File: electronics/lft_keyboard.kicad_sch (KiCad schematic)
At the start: 30 parts, among them SW1 SW_SPST, SW10 SW_SPST, SW11 SW_SPST, SW12 SW_SPST, SW13 SW_SPST, SW14 SW_SPST, SW15 SW_SPST, SW16 SW_SPST, SW17 SW_SPST, SW18 SW_SPST, SW19 SW_SPST, SW2 SW_SPST, SW20 SW_SPST, SW21 SW_SPST, SW22 SW_SPST, SW23 SW_SPST, SW24 SW_SPST, SW25 SW_SPST, SW26 SW_SPST, SW27 SW_SPST, SW28 SW_SPST, SW29 SW_SPST, SW3 SW_SPST, SW4 SW_SPST, SW5 SW_SPST, SW6 SW_SPST, SW7 SW_SPST, SW8 SW_SPST, SW9 SW_SPST, U2 PCA9506DGG

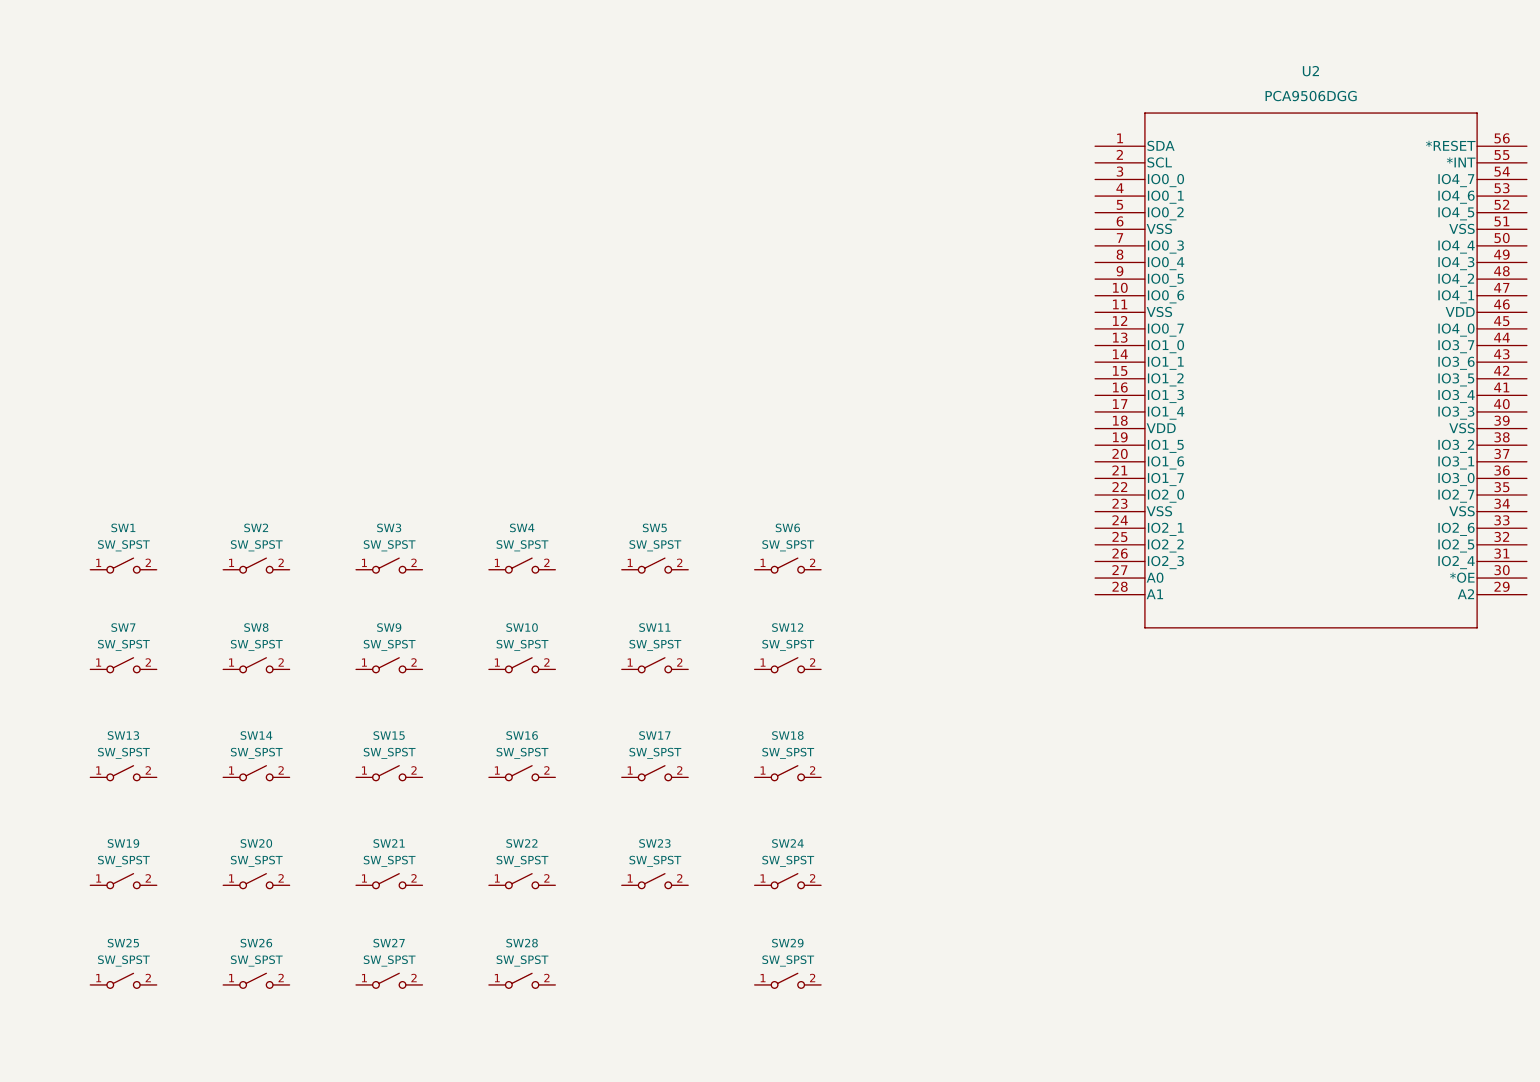
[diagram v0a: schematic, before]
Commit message: ground left keeb switches
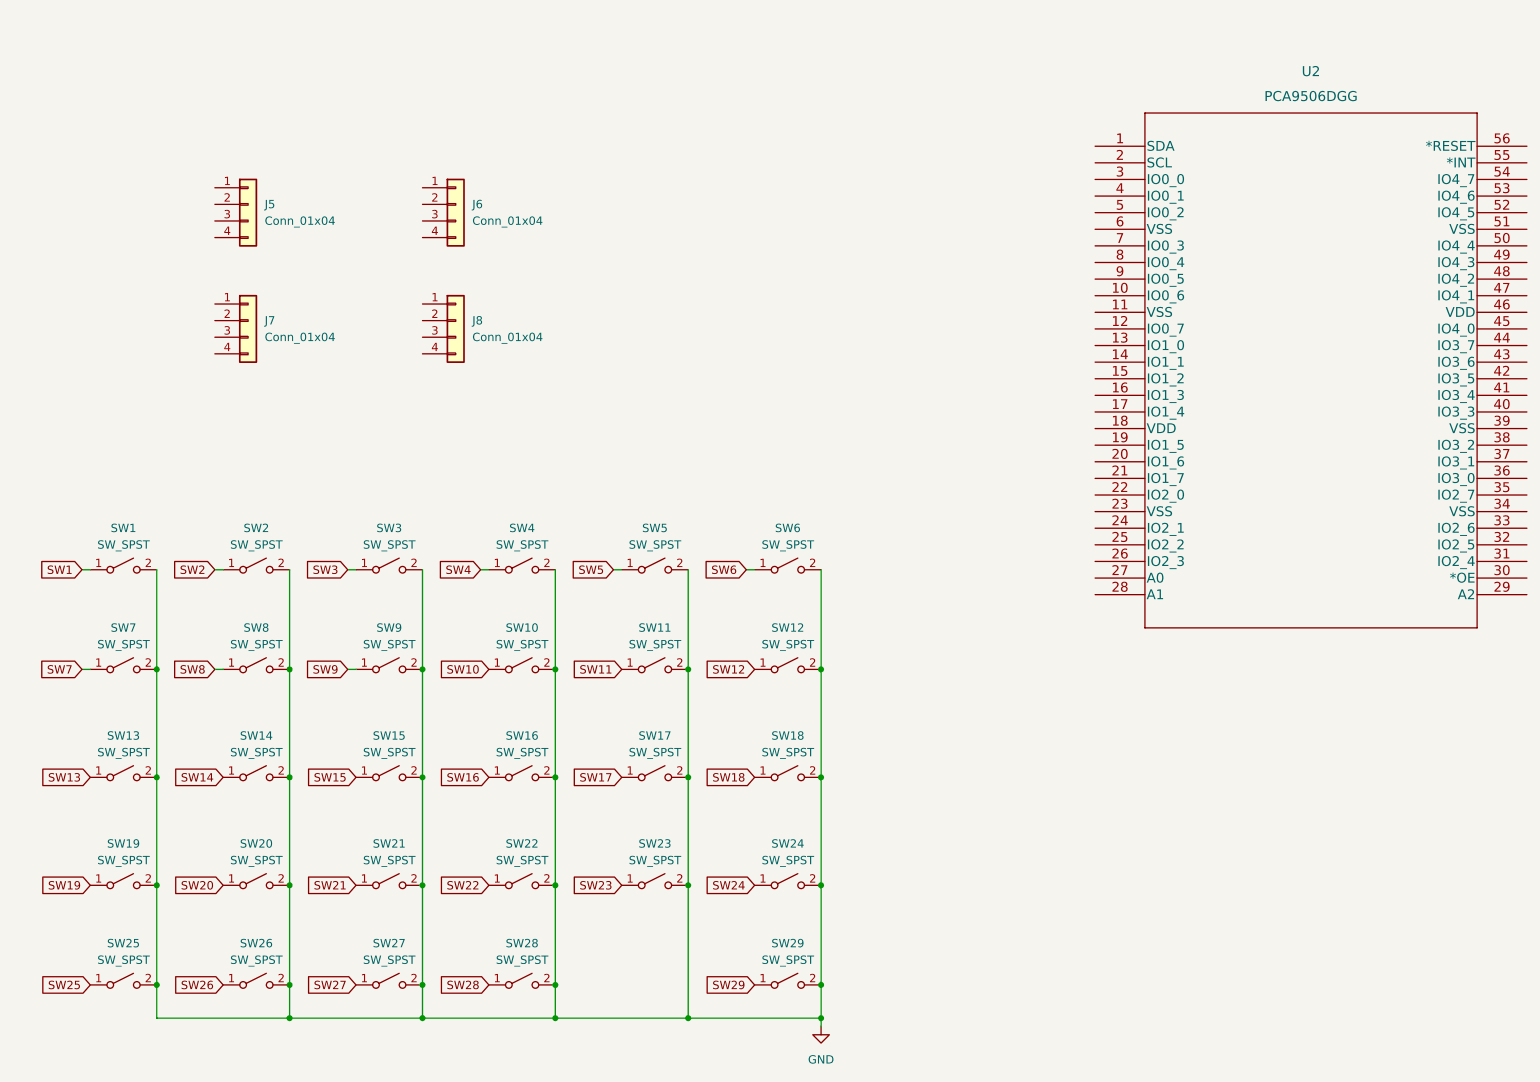
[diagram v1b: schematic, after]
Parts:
- added J5, J6, J7, J8: Conn_01x04, symbol Connector_Generic:Conn_01x04
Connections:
- net SW13: now reaches SW13.1 (A)
- net GND: now reaches SW13.2 (B)
- net GND: now also SW1.2 (B), SW10.2 (B), SW11.2 (B), SW12.2 (B), SW14.2 (B), SW15.2 (B), SW16.2 (B), SW17.2 (B), SW18.2 (B), SW19.2 (B), SW2.2 (B), SW20.2 (B), SW21.2 (B), SW22.2 (B), SW23.2 (B), SW24.2 (B), SW25.2 (B), SW26.2 (B), SW27.2 (B), SW28.2 (B), SW29.2 (B), SW3.2 (B), SW4.2 (B), SW5.2 (B), SW6.2 (B), SW7.2 (B), SW8.2 (B), SW9.2 (B)
- net SW29: now reaches SW29.1 (A)
- net SW28: now reaches SW28.1 (A)
- net SW27: now reaches SW27.1 (A)
- net SW15: now reaches SW15.1 (A)
- net SW23: now reaches SW23.1 (A)
- net SW22: now reaches SW22.1 (A)
- net SW20: now reaches SW20.1 (A)
- net SW25: now reaches SW25.1 (A)
- net SW2: now reaches SW2.1 (A)
- net SW11: now reaches SW11.1 (A)
- net SW12: now reaches SW12.1 (A)
- net SW7: now reaches SW7.1 (A)
- net SW10: now reaches SW10.1 (A)
- net SW14: now reaches SW14.1 (A)
- net SW17: now reaches SW17.1 (A)
- net SW18: now reaches SW18.1 (A)
- net SW19: now reaches SW19.1 (A)
- net SW9: now reaches SW9.1 (A)
- net SW24: now reaches SW24.1 (A)
- net SW26: now reaches SW26.1 (A)
- net SW21: now reaches SW21.1 (A)
- net SW16: now reaches SW16.1 (A)
- net SW4: now reaches SW4.1 (A)
- net SW6: now reaches SW6.1 (A)
- net SW1: now reaches SW1.1 (A)
- net SW8: now reaches SW8.1 (A)
- net SW3: now reaches SW3.1 (A)
- net SW5: now reaches SW5.1 (A)

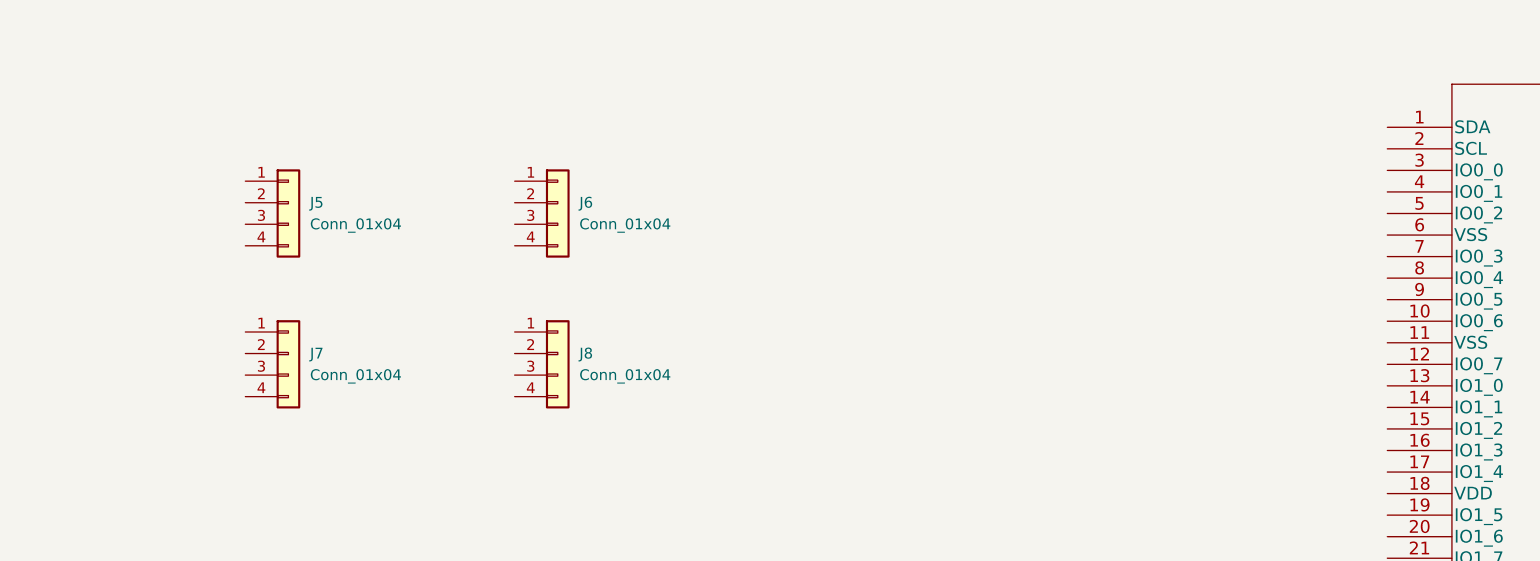
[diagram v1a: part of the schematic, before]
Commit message: label switch nets
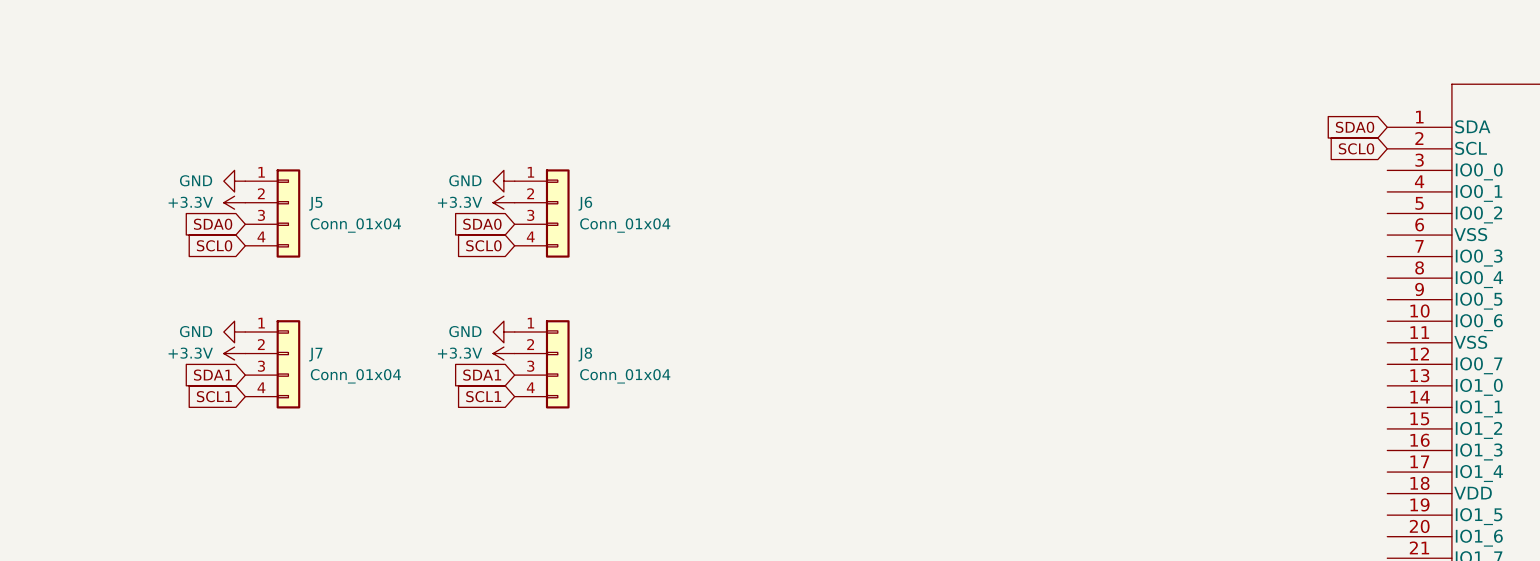
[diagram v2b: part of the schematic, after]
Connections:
- net GND: now also J5.1 (Pin_1), J6.1 (Pin_1), J7.1 (Pin_1), J8.1 (Pin_1)
- net +3V3: now reaches J6.2 (Pin_2)
- net +3V3: now also J5.2 (Pin_2), J7.2 (Pin_2), J8.2 (Pin_2)
- net SDA0: now reaches J6.3 (Pin_3)
- net SDA0: now also J5.3 (Pin_3), U2.1 (SDA)
- net SCL0: now reaches J6.4 (Pin_4)
- net SCL0: now also J5.4 (Pin_4), U2.2 (SCL)
- net SDA1: now reaches J8.3 (Pin_3)
- net SDA1: now also J7.3 (Pin_3)
- net SCL1: now reaches J8.4 (Pin_4)
- net SCL1: now also J7.4 (Pin_4)
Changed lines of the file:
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@@
+    )
+  )
+  (global_label "SCL0" (shape input) (at 80.01 50.8 180) (fields_autoplaced)
+    (effects (font (size 1.27 1.27)) (justify right))
+    (property "Intersheet References" "${INTERSHEET_REFS}" (id 0) (at 72.8798 50.8794 0)
+      (effects (font (size 1.27 1.27)) (justify right) hide)
+    )
+  )
+  (global_label "SDA1" (shape input) (at 48.26 66.04 180) (fields_autoplaced)
+    (effects (font (size 1.27 1.27)) (justify right))
+    (property "Intersheet References" "${INTERSHEET_REFS}" (id 0) (at 41.0693 66.1194 0)
+      (effects (font (size 1.27 1.27)) (justify right) hide)
+    )
+  )
+  (global_label "SDA0" (shape input) (at 80.01 48.26 180) (fields_autoplaced)
+    (effects (font (size 1.27 1.27)) (justify right))
+    (property "Intersheet References" "${INTERSHEET_REFS}" (id 0) (at 72.8193 48.3394 0)
+      (effects (font (size 1.27 1.27)) (justify right) hide)
     )
   )
@@
     )
   )
+  (global_label "SDA0" (shape input) (at 182.88 36.83 180) (fields_autoplaced)
+    (effects (font (size 1.27 1.27)) (justify right))
+    (property "Intersheet References" "${INTERSHEET_REFS}" (id 0) (at 175.6893 36.9094 0)
+      (effects (font (size 1.27 1.27)) (justify right) hide)
+    )
+  )
   (global_label "SW24" (shape input) (at 130.81 149.86 180) (fields_autoplaced)
     (effects (font (size 1.27 1.27)) (justify right))
@@
     )
   )
+  (global_label "SDA0" (shape input) (at 48.26 48.26 180) (fields_autoplaced)
+    (effects (font (size 1.27 1.27)) (justify right))
+    (property "Intersheet References" "${INTERSHEET_REFS}" (id 0) (at 41.0693 48.3394 0)
+      (effects (font (size 1.27 1.27)) (justify right) hide)
+    )
+  )
+  (global_label "SDA1" (shape input) (at 80.01 66.04 180) (fields_autoplaced)
+    (effects (font (size 1.27 1.27)) (justify right))
+    (property "Intersheet References" "${INTERSHEET_REFS}" (id 0) (at 72.8193 66.1194 0)
+      (effects (font (size 1.27 1.27)) (justify right) hide)
+    )
+  )
   (global_label "SW5" (shape input) (at 109.22 101.6 180) (fields_autoplaced)
     (effects (font (size 1.27 1.27)) (justify right))
@@
     )
   )
+  (global_label "SCL0" (shape input) (at 48.26 50.8 180) (fields_autoplaced)
+    (effects (font (size 1.27 1.27)) (justify right))
+    (property "Intersheet References" "${INTERSHEET_REFS}" (id 0) (at 41.1298 50.8794 0)
+      (effects (font (size 1.27 1.27)) (justify right) hide)
+    )
+  )
   (global_label "SW10" (shape input) (at 90.17 116.84 180) (fields_autoplaced)
     (effects (font (size 1.27 1.27)) (justify right))
@@
     )
   )
+  (global_label "SCL1" (shape input) (at 80.01 68.58 180) (fields_autoplaced)
+    (effects (font (size 1.27 1.27)) (justify right))
+    (property "Intersheet References" "${INTERSHEET_REFS}" (id 0) (at 72.8798 68.6594 0)
+      (effects (font (size 1.27 1.27)) (justify right) hide)
+    )
+  )
+  (global_label "SCL0" (shape input) (at 182.88 39.37 180) (fields_autoplaced)
+    (effects (font (size 1.27 1.27)) (justify right))
+    (property "Intersheet References" "${INTERSHEET_REFS}" (id 0) (at 175.7498 39.4494 0)
+      (effects (font (size 1.27 1.27)) (justify right) hide)
+    )
+  )
   (global_label "SW2" (shape input) (at 48.26 101.6 180) (fields_autoplaced)
     (effects (font (size 1.27 1.27)) (justify right))
@@
     (effects (font (size 1.27 1.27)) (justify right))
     (property "Intersheet References" "${INTERSHEET_REFS}" (id 0) (at 62.3569 133.4294 0)
+      (effects (font (size 1.27 1.27)) (justify right) hide)
+    )
+  )
+  (global_label "SCL1" (shape input) (at 48.26 68.58 180) (fields_autoplaced)
+    (effects (font (size 1.27 1.27)) (justify right))
+    (property "Intersheet References" "${INTERSHEET_REFS}" (id 0) (at 41.1298 68.6594 0)
       (effects (font (size 1.27 1.27)) (justify right) hide)
     )
@@
     (pin "2")
   )
+  (symbol (lib_id "power:+3.3V") (at 80.01 63.5 90) (unit 1)
+    (in_bom yes) (on_board yes) (fields_autoplaced)
+    (property "Reference" "#PWR020" (id 0) (at 83.82 63.5 0)
+      (effects (font (size 1.27 1.27)) hide)
+    )
+    (property "Value" "+3.3V" (id 1) (at 76.2 63.4999 90)
+      (effects (font (size 1.27 1.27)) (justify left))
+    )
+    (property "Footprint" "" (id 2) (at 80.01 63.5 0)
+      (effects (font (size 1.27 1.27)) hide)
+    )
+    (property "Datasheet" "" (id 3) (at 80.01 63.5 0)
+      (effects (font (size 1.27 1.27)) hide)
+    )
+    (pin "1")
+  )
   (symbol (lib_name "SW_SPST_8") (lib_id "Kailh:SW_SPST") (at 135.89 165.1 0) (unit 1)
     (in_bom yes) (on_board yes) (fields_autoplaced)
@@
     (pin "2")
   )
+  (symbol (lib_id "power:+3.3V") (at 48.26 63.5 90) (unit 1)
+    (in_bom yes) (on_board yes) (fields_autoplaced)
+    (property "Reference" "#PWR019" (id 0) (at 52.07 63.5 0)
+      (effects (font (size 1.27 1.27)) hide)
+    )
+    (property "Value" "+3.3V" (id 1) (at 44.45 63.4999 90)
+      (effects (font (size 1.27 1.27)) (justify left))
+    )
+    (property "Footprint" "" (id 2) (at 48.26 63.5 0)
+      (effects (font (size 1.27 1.27)) hide)
+    )
+    (property "Datasheet" "" (id 3) (at 48.26 63.5 0)
+      (effects (font (size 1.27 1.27)) hide)
+    )
+    (pin "1")
+  )
   (symbol (lib_id "Connector_Generic:Conn_01x04") (at 85.09 45.72 0) (unit 1)
     (in_bom yes) (on_board yes) (fields_autoplaced)
@@
     (pin "3")
     (pin "4")
+  )
+  (symbol (lib_id "power:GND") (at 80.01 60.96 270) (unit 1)
+    (in_bom yes) (on_board yes) (fields_autoplaced)
+    (property "Reference" "#PWR018" (id 0) (at 73.66 60.96 0)
+      (effects (font (size 1.27 1.27)) hide)
+    )
+    (property "Value" "GND" (id 1) (at 76.2 60.9599 90)
+      (effects (font (size 1.27 1.27)) (justify right))
+    )
+    (property "Footprint" "" (id 2) (at 80.01 60.96 0)
+      (effects (font (size 1.27 1.27)) hide)
+    )
+    (property "Datasheet" "" (id 3) (at 80.01 60.96 0)
+      (effects (font (size 1.27 1.27)) hide)
+    )
+    (pin "1")
   )
   (symbol (lib_name "SW_SPST_10") (lib_id "Kailh:SW_SPST") (at 115.57 149.86 0) (unit 1)
@@
     (pin "2")
   )
+  (symbol (lib_id "power:+3.3V") (at 80.01 45.72 90) (unit 1)
+    (in_bom yes) (on_board yes) (fields_autoplaced)
+    (property "Reference" "#PWR016" (id 0) (at 83.82 45.72 0)
+      (effects (font (size 1.27 1.27)) hide)
+    )
+    (property "Value" "+3.3V" (id 1) (at 76.2 45.7199 90)
+      (effects (font (size 1.27 1.27)) (justify left))
+    )
+    (property "Footprint" "" (id 2) (at 80.01 45.72 0)
+      (effects (font (size 1.27 1.27)) hide)
+    )
+    (property "Datasheet" "" (id 3) (at 80.01 45.72 0)
+      (effects (font (size 1.27 1.27)) hide)
+    )
+    (pin "1")
+  )
   (symbol (lib_id "Connector_Generic:Conn_01x04") (at 53.34 63.5 0) (unit 1)
     (in_bom yes) (on_board yes) (fields_autoplaced)
@@
     (pin "2")
   )
+  (symbol (lib_id "power:GND") (at 48.26 60.96 270) (unit 1)
+    (in_bom yes) (on_board yes) (fields_autoplaced)
+    (property "Reference" "#PWR017" (id 0) (at 41.91 60.96 0)
+      (effects (font (size 1.27 1.27)) hide)
+    )
+    (property "Value" "GND" (id 1) (at 44.45 60.9599 90)
+      (effects (font (size 1.27 1.27)) (justify right))
+    )
+    (property "Footprint" "" (id 2) (at 48.26 60.96 0)
+      (effects (font (size 1.27 1.27)) hide)
+    )
+    (property "Datasheet" "" (id 3) (at 48.26 60.96 0)
+      (effects (font (size 1.27 1.27)) hide)
+    )
+    (pin "1")
+  )
   (symbol (lib_name "SW_SPST_1") (lib_id "Kailh:SW_SPST") (at 54.61 165.1 0) (unit 1)
     (in_bom yes) (on_board yes) (fields_autoplaced)
@@
     (pin "2")
   )
+  (symbol (lib_id "power:GND") (at 48.26 43.18 270) (unit 1)
+    (in_bom yes) (on_board yes) (fields_autoplaced)
+    (property "Reference" "#PWR013" (id 0) (at 41.91 43.18 0)
+      (effects (font (size 1.27 1.27)) hide)
+    )
+    (property "Value" "GND" (id 1) (at 44.45 43.1799 90)
+      (effects (font (size 1.27 1.27)) (justify right))
+    )
+    (property "Footprint" "" (id 2) (at 48.26 43.18 0)
+      (effects (font (size 1.27 1.27)) hide)
+    )
+    (property "Datasheet" "" (id 3) (at 48.26 43.18 0)
+      (effects (font (size 1.27 1.27)) hide)
+    )
+    (pin "1")
+  )
   (symbol (lib_name "SW_SPST_21") (lib_id "Kailh:SW_SPST") (at 95.25 133.35 0) (unit 1)
     (in_bom yes) (on_board yes) (fields_autoplaced)
@@
     (pin "2")
   )
+  (symbol (lib_id "power:+3.3V") (at 48.26 45.72 90) (unit 1)
+    (in_bom yes) (on_board yes) (fields_autoplaced)
+    (property "Reference" "#PWR015" (id 0) (at 52.07 45.72 0)
+      (effects (font (size 1.27 1.27)) hide)
+    )
+    (property "Value" "+3.3V" (id 1) (at 44.45 45.7199 90)
+      (effects (font (size 1.27 1.27)) (justify left))
+    )
+    (property "Footprint" "" (id 2) (at 48.26 45.72 0)
+      (effects (font (size 1.27 1.27)) hide)
+    )
+    (property "Datasheet" "" (id 3) (at 48.26 45.72 0)
+      (effects (font (size 1.27 1.27)) hide)
+    )
+    (pin "1")
+  )
   (symbol (lib_name "SW_SPST_22") (lib_id "Kailh:SW_SPST") (at 95.25 101.6 0) (unit 1)
     (in_bom yes) (on_board yes) (fields_autoplaced)
@@
     (pin "2")
   )
+  (symbol (lib_id "power:GND") (at 80.01 43.18 270) (unit 1)
+    (in_bom yes) (on_board yes) (fields_autoplaced)
+    (property "Reference" "#PWR014" (id 0) (at 73.66 43.18 0)
+      (effects (font (size 1.27 1.27)) hide)
+    )
+    (property "Value" "GND" (id 1) (at 76.2 43.1799 90)
+      (effects (font (size 1.27 1.27)) (justify right))
+    )
+    (property "Footprint" "" (id 2) (at 80.01 43.18 0)
+      (effects (font (size 1.27 1.27)) hide)
+    )
+    (property "Datasheet" "" (id 3) (at 80.01 43.18 0)
+      (effects (font (size 1.27 1.27)) hide)
+    )
+    (pin "1")
+  )
   (symbol (lib_name "SW_SPST_17") (lib_id "Kailh:SW_SPST") (at 74.93 101.6 0) (unit 1)
